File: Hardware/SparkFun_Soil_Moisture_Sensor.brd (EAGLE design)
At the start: 22.9 x 61 mm, 13 parts, among them Q1 2N3904

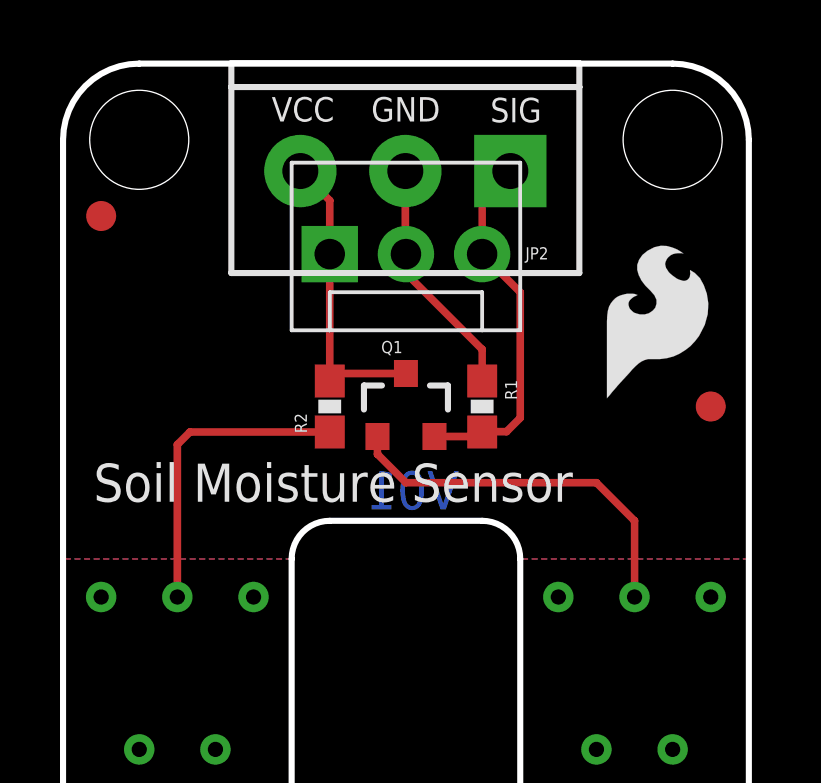
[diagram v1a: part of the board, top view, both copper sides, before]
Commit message: Ready for QC checklist
thickened traces, few minor aesthetic changes. Updated version #.
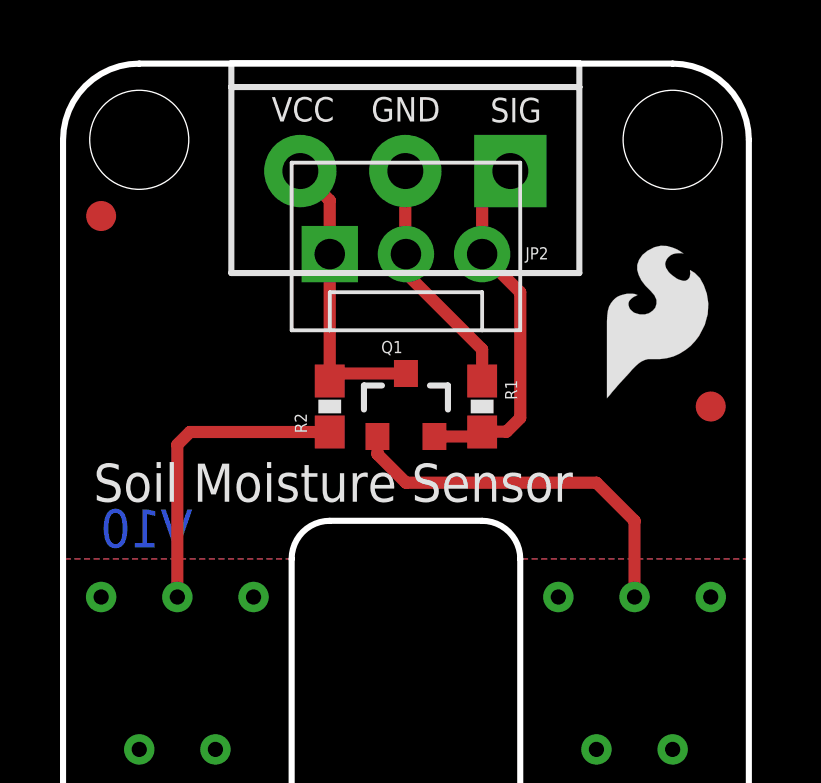
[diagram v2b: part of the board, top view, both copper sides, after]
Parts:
- JP1, JP2: value (none) -> DNP
- moved LOGO2 7.73 mm to (20.3, 54.6)
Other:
- board text added: "V10"
- board text removed: "V01"
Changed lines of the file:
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@@
 <layer number="45" name="Holes" color="7" fill="1" visible="yes" active="yes"/>
 <layer number="46" name="Milling" color="3" fill="1" visible="no" active="yes"/>
-<layer number="47" name="Measures" color="7" fill="1" visible="no" active="yes"/>
+<layer number="47" name="Measures" color="7" fill="1" visible="yes" active="yes"/>
 <layer number="48" name="Document" color="7" fill="1" visible="no" active="yes"/>
 <layer number="49" name="Reference" color="7" fill="1" visible="no" active="yes"/>
@@
 <board>
 <plain>
-<dimension x1="22.86" y1="60.96" x2="22.86" y2="0" x3="30.48" y3="30.48" textsize="1.778" textratio="15" layer="51" unit="inch"/>
+<dimension x1="22.86" y1="60.96" x2="22.86" y2="0" x3="30.48" y3="30.48" textsize="1.778" textratio="15" layer="47" unit="inch"/>
 <wire x1="2.54" y1="60.96" x2="0" y2="58.42" width="0.2032" layer="20" curve="90"/>
 <wire x1="0" y1="58.42" x2="0" y2="7.62" width="0.2032" layer="20"/>
-<dimension x1="0" y1="60.96" x2="22.86" y2="60.96" x3="11.43" y3="64.77" textsize="1.778" textratio="15" layer="51" unit="inch"/>
+<dimension x1="0" y1="60.96" x2="22.86" y2="60.96" x3="11.43" y3="64.77" textsize="1.778" textratio="15" layer="47" unit="inch"/>
 <wire x1="2.54" y1="60.96" x2="20.32" y2="60.96" width="0.2032" layer="20"/>
 <wire x1="20.32" y1="60.96" x2="22.86" y2="58.42" width="0.2032" layer="20" curve="-90"/>
@@
 <text x="12.7" y="59.563" size="1.016" layer="22" font="vector" ratio="15" rot="SMR0">GND</text>
 <text x="19.05" y="-10.16" size="1.778" layer="51" font="vector" ratio="10">Joel Bartlett</text>
-<text x="13.208" y="46.101" size="1.27" layer="16" font="vector" ratio="15" rot="SMR0">V01</text>
-<dimension x1="7.62" y1="7.62" x2="15.24" y2="7.62" x3="11.43" y3="1.27" textsize="1.27" textratio="15" layer="51" unit="inch"/>
-<dimension x1="2.54" y1="58.42" x2="20.32" y2="58.42" x3="11.43" y3="62.23" textsize="1.27" textratio="15" layer="51" unit="inch"/>
+<dimension x1="7.62" y1="7.62" x2="15.24" y2="7.62" x3="11.43" y3="1.27" textsize="1.27" textratio="15" layer="47" unit="inch"/>
+<dimension x1="2.54" y1="58.42" x2="20.32" y2="58.42" x3="11.43" y3="62.23" textsize="1.27" textratio="15" layer="47" unit="inch"/>
 <wire x1="0" y1="44.45" x2="7.62" y2="44.45" width="0.254" layer="29"/>
 <wire x1="7.62" y1="44.45" x2="7.62" y2="7.62" width="0.254" layer="29"/>
@@
 <vertex x="22.86" y="44.45"/>
 </polygon>
+<text x="21.844" y="46.355" size="1.27" layer="22" font="vector" ratio="15" rot="MR0">Soil Moisture Sensor</text>
+<text x="4.318" y="44.831" size="1.27" layer="16" font="vector" ratio="15" rot="SMR0">V10</text>
 </plain>
 <attributes>
@@
 </element>
 <element name="LOGO1" library="SparkFun-Aesthetics" package="SFE_LOGO_NAME_FLAME_.1" value="SFE_LOGO_NAME_FLAME.1_INCH" x="17.78" y="48.26" rot="MR0"/>
-<element name="LOGO2" library="SparkFun-Aesthetics" package="OSHW-LOGO-S" value="OSHW-LOGOS" x="19.05" y="46.99" rot="MR0"/>
+<element name="LOGO2" library="SparkFun-Aesthetics" package="OSHW-LOGO-S" value="OSHW-LOGOS" x="20.32" y="54.61" rot="MR0"/>
 <element name="U$4" library="SparkFun-Aesthetics" package="SFE_LOGO_FLAME_.2" value="" x="17.78" y="49.53"/>
-<element name="JP1" library="SparkFun-Connectors" package="MOLEX-1X3" value="" x="8.89" y="54.61"/>
-<element name="JP2" library="SparkFun-Connectors" package="SCREWTERMINAL-3.5MM-3" value="" x="14.9098" y="57.3786" rot="R180"/>
+<element name="JP1" library="SparkFun-Connectors" package="MOLEX-1X3" value="DNP" x="8.89" y="54.61"/>
+<element name="JP2" library="SparkFun-Connectors" package="SCREWTERMINAL-3.5MM-3" value="DNP" x="14.9098" y="57.3786" rot="R180"/>
 <element name="STANDOFF1" library="SparkFun-Electromechanical" package="STAND-OFF" value="STAND-OFF" x="2.54" y="58.42"/>
 <element name="STANDOFF2" library="SparkFun-Electromechanical" package="STAND-OFF" value="STAND-OFF" x="20.32" y="58.42"/>
@@
 <contactref element="Q1" pad="2"/>
 <contactref element="R1" pad="2"/>
-<wire x1="12.38" y1="48.53" x2="13.82" y2="48.53" width="0.254" layer="1"/>
+<wire x1="12.38" y1="48.53" x2="13.82" y2="48.53" width="0.4064" layer="1"/>
 <wire x1="13.82" y1="48.53" x2="13.97" y2="48.68" width="0.254" layer="1"/>
 <contactref element="JP1" pad="3"/>
 <contactref element="JP2" pad="1"/>
-<wire x1="14.9098" y1="57.3786" x2="13.97" y2="56.4388" width="0.254" layer="1"/>
-<wire x1="13.97" y1="56.4388" x2="13.97" y2="54.61" width="0.254" layer="1"/>
-<wire x1="13.97" y1="54.61" x2="15.24" y2="53.34" width="0.254" layer="1"/>
-<wire x1="15.24" y1="53.34" x2="15.24" y2="49.149" width="0.254" layer="1"/>
-<wire x1="15.24" y1="49.149" x2="14.7828" y2="48.6918" width="0.254" layer="1"/>
-<wire x1="14.7828" y1="48.6918" x2="13.9818" y2="48.6918" width="0.254" layer="1"/>
+<wire x1="14.9098" y1="57.3786" x2="13.97" y2="56.4388" width="0.4064" layer="1"/>
+<wire x1="13.97" y1="56.4388" x2="13.97" y2="54.61" width="0.4064" layer="1"/>
+<wire x1="13.97" y1="54.61" x2="15.24" y2="53.34" width="0.4064" layer="1"/>
+<wire x1="15.24" y1="53.34" x2="15.24" y2="49.149" width="0.4064" layer="1"/>
+<wire x1="15.24" y1="49.149" x2="14.7828" y2="48.6918" width="0.4064" layer="1"/>
+<wire x1="14.7828" y1="48.6918" x2="13.9818" y2="48.6918" width="0.4064" layer="1"/>
 <wire x1="13.9818" y1="48.6918" x2="13.97" y2="48.68" width="0.254" layer="1"/>
 </signal>
@@
 <contactref element="R2" pad="2"/>
 <wire x1="8.89" y1="50.38" x2="9.14" y2="50.63" width="0.254" layer="1"/>
-<wire x1="9.14" y1="50.63" x2="11.43" y2="50.63" width="0.254" layer="1"/>
+<wire x1="9.14" y1="50.63" x2="11.43" y2="50.63" width="0.4064" layer="1"/>
 <contactref element="JP1" pad="1"/>
 <contactref element="JP2" pad="3"/>
-<wire x1="7.9098" y1="57.3786" x2="8.89" y2="56.3984" width="0.254" layer="1"/>
-<wire x1="8.89" y1="56.3984" x2="8.89" y2="54.61" width="0.254" layer="1"/>
-<wire x1="8.89" y1="54.61" x2="8.89" y2="50.38" width="0.254" layer="1"/>
+<wire x1="7.9098" y1="57.3786" x2="8.89" y2="56.3984" width="0.4064" layer="1"/>
+<wire x1="8.89" y1="56.3984" x2="8.89" y2="54.61" width="0.4064" layer="1"/>
+<wire x1="8.89" y1="54.61" x2="8.89" y2="50.38" width="0.4064" layer="1"/>
 </signal>
 <signal name="GND">
@@
 <contactref element="JP2" pad="2"/>
 <contactref element="JP1" pad="2"/>
-<wire x1="11.4098" y1="57.3786" x2="11.4098" y2="54.6302" width="0.254" layer="1"/>
+<wire x1="11.4098" y1="57.3786" x2="11.4098" y2="54.6302" width="0.4064" layer="1"/>
 <wire x1="11.4098" y1="54.6302" x2="11.43" y2="54.61" width="0.254" layer="1"/>
-<wire x1="11.43" y1="54.61" x2="11.43" y2="53.975" width="0.254" layer="1"/>
-<wire x1="11.43" y1="53.975" x2="13.97" y2="51.435" width="0.254" layer="1"/>
-<wire x1="13.97" y1="51.435" x2="13.97" y2="50.38" width="0.254" layer="1"/>
+<wire x1="11.43" y1="54.61" x2="11.43" y2="53.975" width="0.4064" layer="1"/>
+<wire x1="11.43" y1="53.975" x2="13.97" y2="51.435" width="0.4064" layer="1"/>
+<wire x1="13.97" y1="51.435" x2="13.97" y2="50.38" width="0.4064" layer="1"/>
 </signal>
 <signal name="PROBE1">
@@
 <via x="17.78" y="17.78" extent="1-16" drill="0.508"/>
 <via x="20.32" y="17.78" extent="1-16" drill="0.508"/>
-<wire x1="10.48" y1="48.53" x2="10.48" y2="47.94" width="0.254" layer="1"/>
-<wire x1="10.48" y1="47.94" x2="11.43" y2="46.99" width="0.254" layer="1"/>
-<wire x1="11.43" y1="46.99" x2="17.78" y2="46.99" width="0.254" layer="1"/>
-<wire x1="19.05" y1="43.18" x2="19.05" y2="45.72" width="0.254" layer="1"/>
-<wire x1="19.05" y1="45.72" x2="17.78" y2="46.99" width="0.254" layer="1"/>
+<wire x1="10.48" y1="48.53" x2="10.48" y2="47.94" width="0.4064" layer="1"/>
+<wire x1="10.48" y1="47.94" x2="11.43" y2="46.99" width="0.4064" layer="1"/>
+<wire x1="11.43" y1="46.99" x2="17.78" y2="46.99" width="0.4064" layer="1"/>
+<wire x1="19.05" y1="43.18" x2="19.05" y2="45.72" width="0.4064" layer="1"/>
+<wire x1="19.05" y1="45.72" x2="17.78" y2="46.99" width="0.4064" layer="1"/>
 </signal>
 <signal name="PROBE2">
@@
 <vertex x="7.62" y="44.45"/>
 </polygon>
-<wire x1="3.81" y1="48.26" x2="3.81" y2="43.18" width="0.254" layer="1"/>
+<wire x1="3.81" y1="48.26" x2="3.81" y2="43.18" width="0.4064" layer="1"/>
 <via x="3.81" y="43.18" extent="1-16" drill="0.508"/>
 <polygon width="0.254" layer="16">
@@
 <via x="2.54" y="38.1" extent="1-16" drill="0.508"/>
 <via x="5.08" y="38.1" extent="1-16" drill="0.508"/>
-<wire x1="8.89" y1="48.68" x2="4.23" y2="48.68" width="0.254" layer="1"/>
-<wire x1="4.23" y1="48.68" x2="3.81" y2="48.26" width="0.254" layer="1"/>
+<wire x1="8.89" y1="48.68" x2="4.23" y2="48.68" width="0.4064" layer="1"/>
+<wire x1="4.23" y1="48.68" x2="3.81" y2="48.26" width="0.4064" layer="1"/>
 </signal>
 </signals>

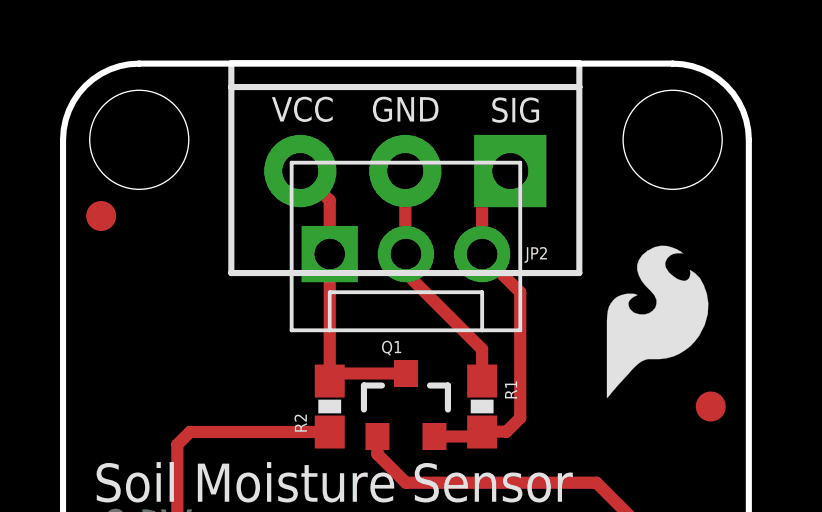
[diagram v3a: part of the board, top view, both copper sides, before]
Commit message: Added Locking 3-pin 3.5mm footprint
Added Locking 3-pin 3.5mm footprint for selective soldering.
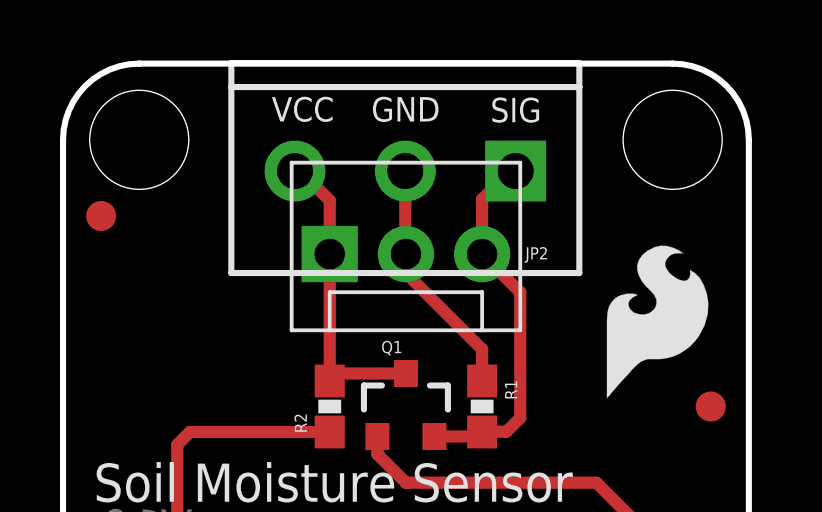
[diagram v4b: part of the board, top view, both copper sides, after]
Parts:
- JP2: value DNP -> (none); device SparkFun-Connectors:SCREWTERMINAL-3.5MM-3 -> SparkFun-Connectors:SCREWTERMINAL-3.5MM-3_LOCK.007S
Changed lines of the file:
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@@
 <setting verticaltext="up"/>
 </settings>
-<grid distance="0.05" unitdist="inch" unit="inch" style="lines" multiple="1" display="yes" altdistance="0.005" altunitdist="inch" altunit="inch"/>
+<grid distance="0.05" unitdist="inch" unit="inch" style="lines" multiple="1" display="yes" altdistance="0.001" altunitdist="inch" altunit="inch"/>
 <layers>
 <layer number="1" name="Top" color="4" fill="1" visible="yes" active="yes"/>
@@
 <element name="U$4" library="SparkFun-Aesthetics" package="SFE_LOGO_FLAME_.2" value="" x="17.78" y="49.53"/>
 <element name="JP1" library="SparkFun-Connectors" package="MOLEX-1X3" value="DNP" x="8.89" y="54.61"/>
-<element name="JP2" library="SparkFun-Connectors" package="SCREWTERMINAL-3.5MM-3" value="DNP" x="14.9098" y="57.3786" rot="R180"/>
 <element name="STANDOFF1" library="SparkFun-Electromechanical" package="STAND-OFF" value="STAND-OFF" x="2.54" y="58.42"/>
 <element name="STANDOFF2" library="SparkFun-Electromechanical" package="STAND-OFF" value="STAND-OFF" x="20.32" y="58.42"/>
 <element name="FID1" library="SparkFun-Aesthetics" package="FIDUCIAL-1X2" value="FIDUCIAL1X2" x="1.27" y="55.88"/>
 <element name="FID2" library="SparkFun-Aesthetics" package="FIDUCIAL-1X2" value="FIDUCIAL1X2" x="21.59" y="49.53"/>
+<element name="JP2" library="SparkFun-Connectors" package="SCREWTERMINAL-3.5MM-3_LOCK.007S" value="" x="14.9098" y="57.3786" rot="R180">
+<attribute name="PROD_ID" value="CONN-08288" x="14.9098" y="57.3786" size="1.778" layer="27" font="vector" ratio="15" rot="R180" display="off"/>
+</element>
 </elements>
 <signals>
@@
 <wire x1="13.82" y1="48.53" x2="13.97" y2="48.68" width="0.254" layer="1"/>
 <contactref element="JP1" pad="3"/>
-<contactref element="JP2" pad="1"/>
-<wire x1="14.9098" y1="57.3786" x2="13.97" y2="56.4388" width="0.4064" layer="1"/>
 <wire x1="13.97" y1="56.4388" x2="13.97" y2="54.61" width="0.4064" layer="1"/>
 <wire x1="13.97" y1="54.61" x2="15.24" y2="53.34" width="0.4064" layer="1"/>
@@
 <wire x1="14.7828" y1="48.6918" x2="13.9818" y2="48.6918" width="0.4064" layer="1"/>
 <wire x1="13.9818" y1="48.6918" x2="13.97" y2="48.68" width="0.254" layer="1"/>
+<contactref element="JP2" pad="1"/>
+<wire x1="13.97" y1="56.4388" x2="14.9098" y2="57.3786" width="0.4064" layer="1"/>
+<wire x1="14.9098" y1="57.3786" x2="15.0876" y2="57.3786" width="0.4064" layer="1"/>
 </signal>
 <signal name="VCC">
@@
 <wire x1="9.14" y1="50.63" x2="11.43" y2="50.63" width="0.4064" layer="1"/>
 <contactref element="JP1" pad="1"/>
-<contactref element="JP2" pad="3"/>
-<wire x1="7.9098" y1="57.3786" x2="8.89" y2="56.3984" width="0.4064" layer="1"/>
 <wire x1="8.89" y1="56.3984" x2="8.89" y2="54.61" width="0.4064" layer="1"/>
 <wire x1="8.89" y1="54.61" x2="8.89" y2="50.38" width="0.4064" layer="1"/>
+<contactref element="JP2" pad="3"/>
+<wire x1="8.89" y1="56.3984" x2="7.9098" y2="57.3786" width="0.4064" layer="1"/>
+<wire x1="7.9098" y1="57.3786" x2="7.732" y2="57.3786" width="0.4064" layer="1"/>
 </signal>
 <signal name="GND">
 <contactref element="R1" pad="1"/>
-<contactref element="JP2" pad="2"/>
 <contactref element="JP1" pad="2"/>
-<wire x1="11.4098" y1="57.3786" x2="11.4098" y2="54.6302" width="0.4064" layer="1"/>
 <wire x1="11.4098" y1="54.6302" x2="11.43" y2="54.61" width="0.254" layer="1"/>
 <wire x1="11.43" y1="54.61" x2="11.43" y2="53.975" width="0.4064" layer="1"/>
 <wire x1="11.43" y1="53.975" x2="13.97" y2="51.435" width="0.4064" layer="1"/>
 <wire x1="13.97" y1="51.435" x2="13.97" y2="50.38" width="0.4064" layer="1"/>
+<contactref element="JP2" pad="2"/>
+<wire x1="11.4098" y1="54.6302" x2="11.4098" y2="57.3786" width="0.4064" layer="1"/>
 </signal>
 <signal name="PROBE1">
